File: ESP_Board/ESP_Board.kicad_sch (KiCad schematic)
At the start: 49 parts, among them J1 USB_C_Receptacle_USB2.0_14P, J2 Conn_01x18_Pin, J3 Conn_01x18_Pin, SW1 SW_Push, SW2 SW_Push, U1 ESP32-S3, U2 AMS1117, U3 W25Q128JVSIQ, Y1 C1E-40.000-8-1010-R

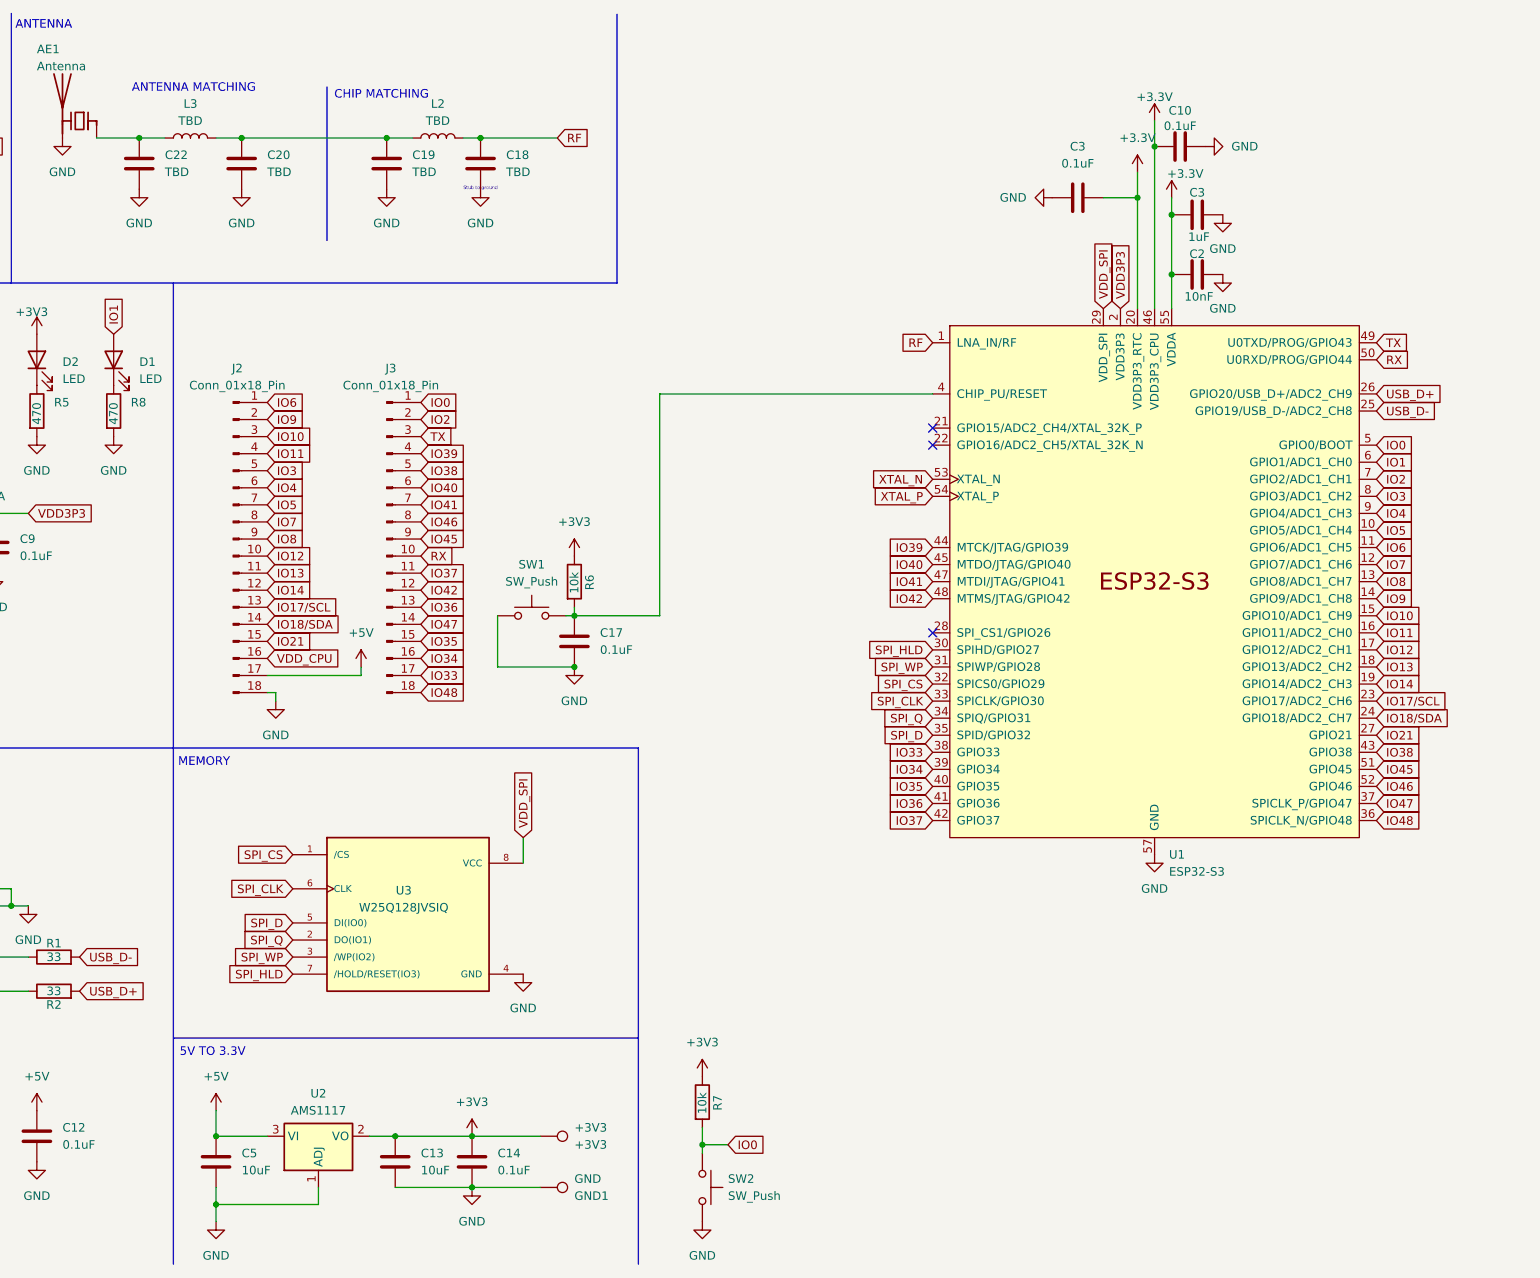
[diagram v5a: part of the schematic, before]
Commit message: Clean up schematic
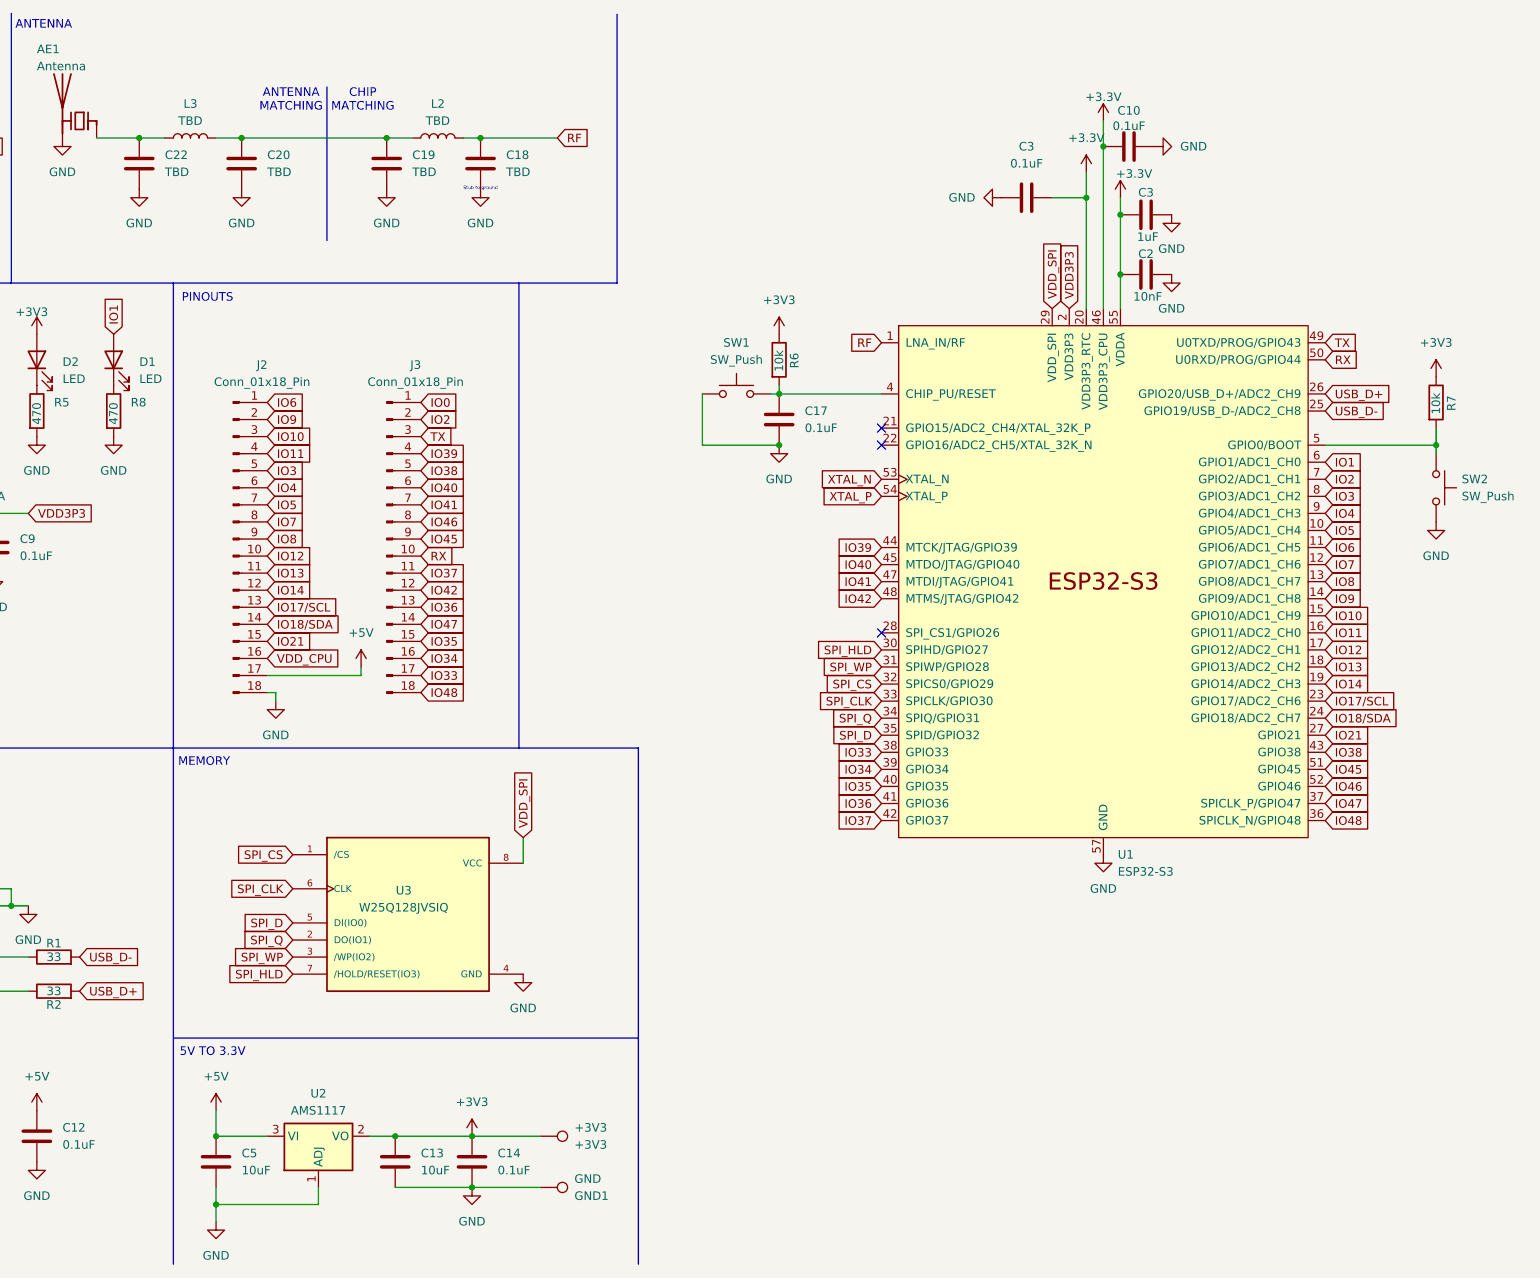
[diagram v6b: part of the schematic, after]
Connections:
- net IO0: no longer R7.2, SW2.1, U1.5 (GPIO0/BOOT)
- new net: R7.2, SW2.1, U1.5 (GPIO0/BOOT)
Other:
- note added: "PINOUTS"
- moved on the sheet: 1uF, C10, C17, C2, C3, R6, R7, SW1, SW2, U1

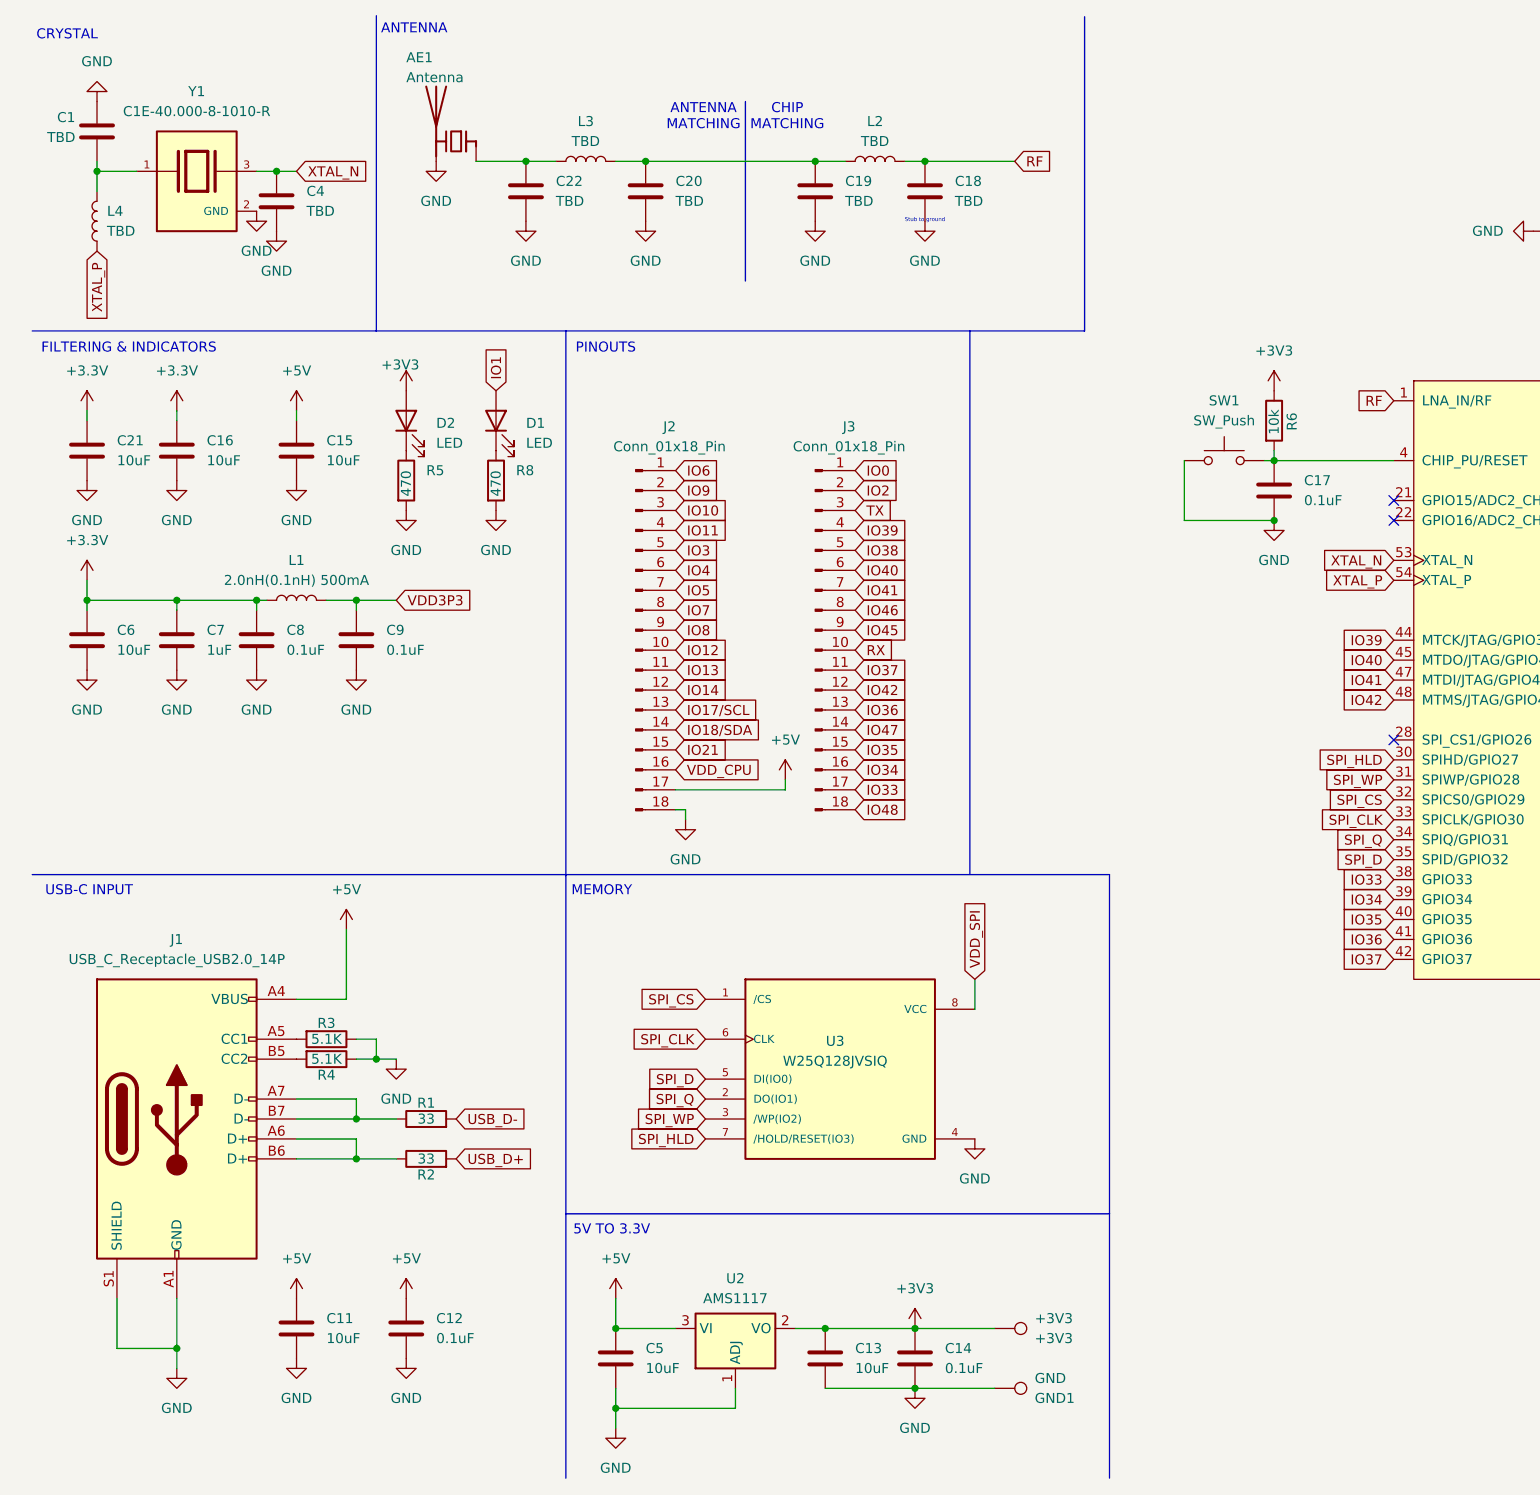
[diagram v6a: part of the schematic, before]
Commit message: Add 32k oscillator + antenna
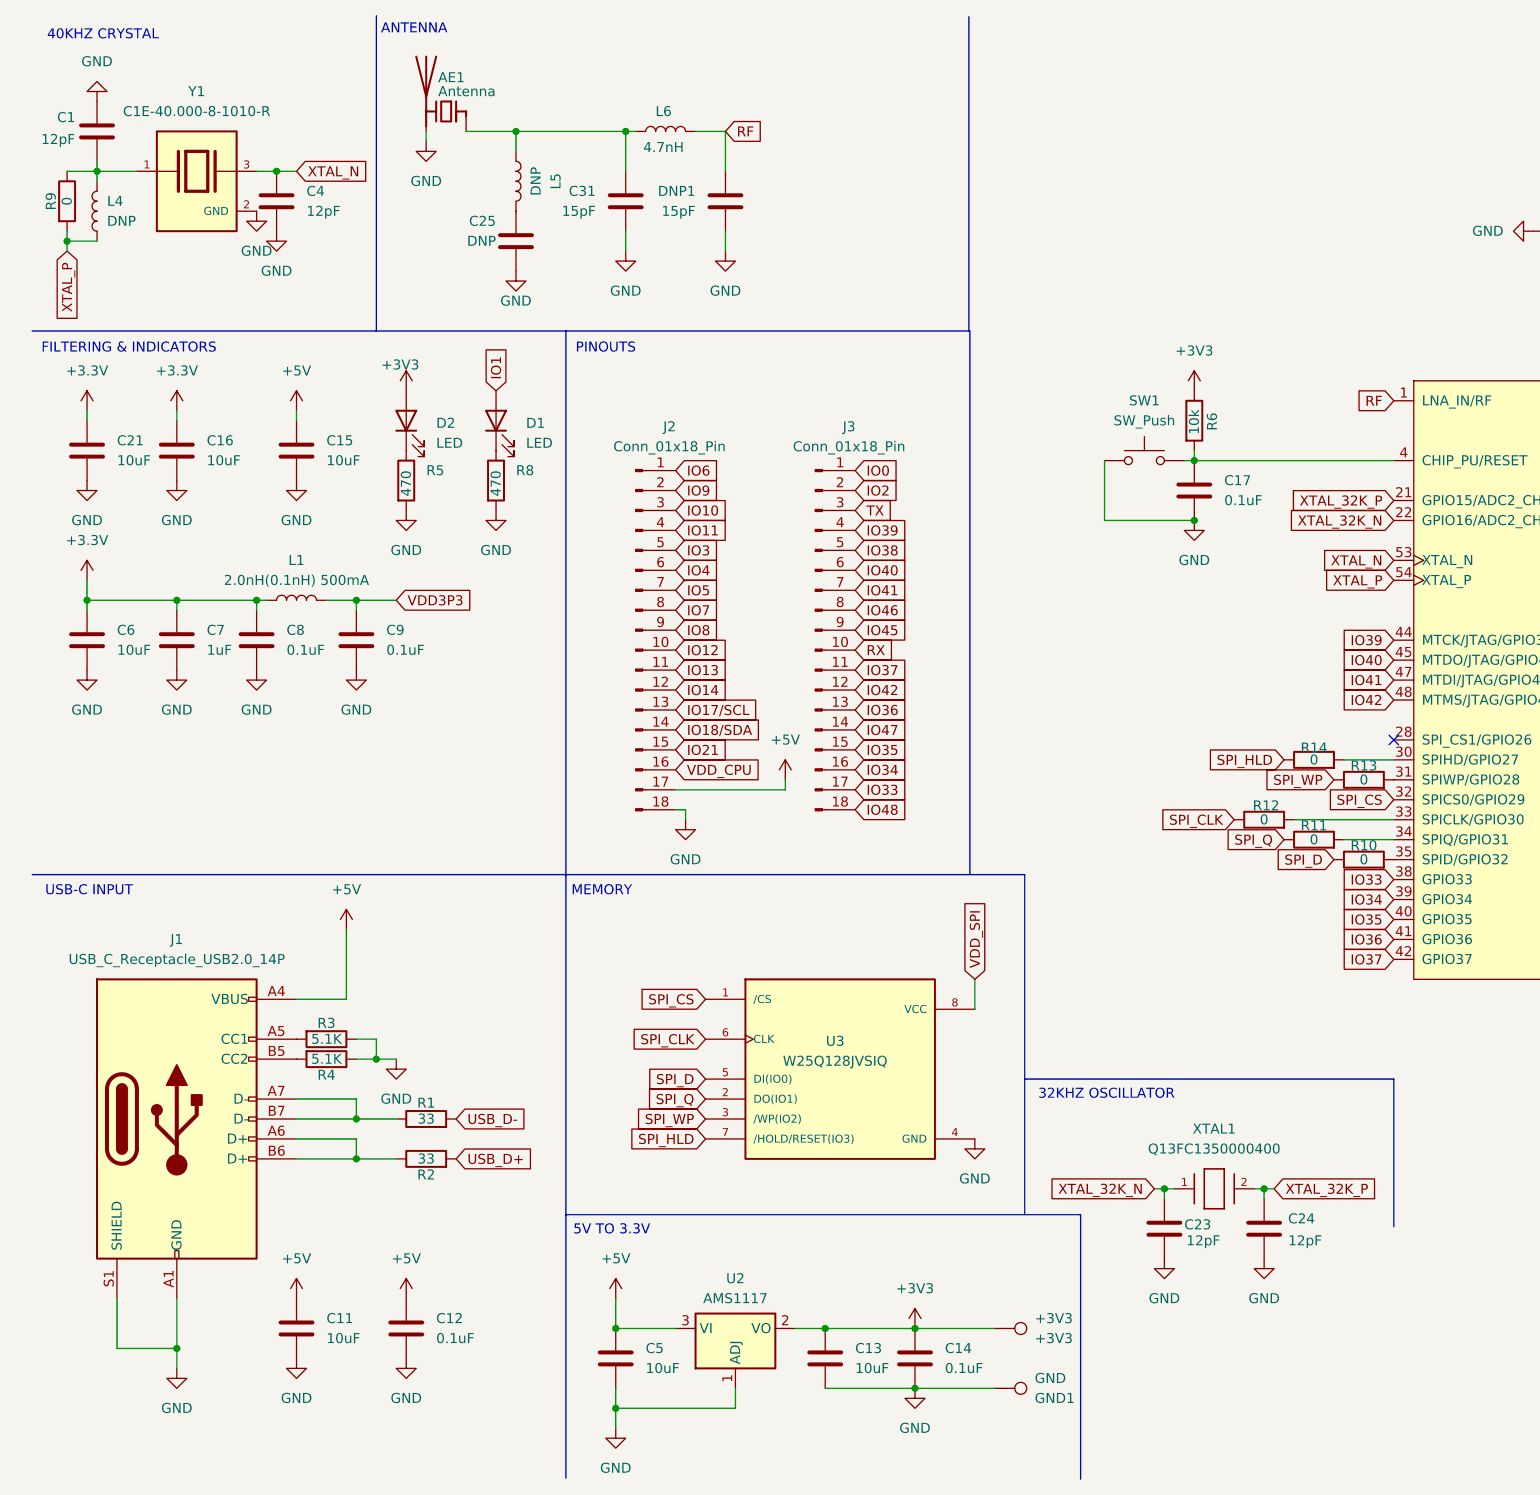
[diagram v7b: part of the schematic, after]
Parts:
- removed C18, C19, C20, C22: TBD, symbol Device:C
- removed L2, L3: TBD, symbol Device:L
- added C23, C24: 12pF, symbol Device:C
- added C25: DNP, Capacitor_SMD:C_0402_1005Metric, symbol Device:C
- added C31, DNP1: 15pF, Capacitor_SMD:C_0402_1005Metric, symbol Device:C
- added L5: DNP, Inductor_SMD:L_0402_1005Metric, symbol Device:L
- added L6: 4.7nH, Inductor_SMD:L_0402_1005Metric, symbol Device:L
- added R10, R11, R12, R13, R14, R9: 0, symbol Device:R
- added XTAL1: Q13FC1350000400, symbol Necessary_Imports:Q13FC1350000400
- C1, C4: value TBD -> 12pF
- L4: value TBD -> DNP
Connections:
- net GND: now also C23.2, C24.2, C25.2, C31.2, DNP1.2
- net RF: now also DNP1.1, L6.1
- net SPI_CLK: now also R12.1; no longer U1.33 (SPICLK/GPIO30)
- net SPI_D: now also R10.1; no longer U1.35 (SPID/GPIO32)
- net SPI_HLD: now also R14.1; no longer U1.30 (SPIHD/GPIO27)
- net SPI_Q: now also R11.1; no longer U1.34 (SPIQ/GPIO31)
- net SPI_WP: now also R13.1; no longer U1.31 (SPIWP/GPIO28)
- net XTAL_P: now also R9.2
- net at C1.2, L4.2, Y1.1: now also R9.1
- net at AE1.1 (FEED): now also C31.1, L5.2, L6.2
- net XTAL_32K_P: now reaches U1.21 (GPIO15/ADC2_CH4/XTAL_32K_P)
- net XTAL_32K_P: now also C24.1, XTAL1.2
- net XTAL_32K_N: now reaches U1.22 (GPIO16/ADC2_CH5/XTAL_32K_N)
- net XTAL_32K_N: now also C23.1, XTAL1.1
- new net: C25.1, L5.1
- new net: R14.2, U1.30 (SPIHD/GPIO27)
- new net: R11.2, U1.34 (SPIQ/GPIO31)
- new net: R12.2, U1.33 (SPICLK/GPIO30)
- new net: R10.2, U1.35 (SPID/GPIO32)
- new net: R13.2, U1.31 (SPIWP/GPIO28)
- no-connect marks 3 -> 1
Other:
- note added: "32KHZ OSCILLATOR"
- note added: "40KHZ CRYSTAL"
- note removed: "ANTENNA MATCHING"
- note removed: "CHIP MATCHING"
- note removed: "CRYSTAL"
- note removed: "Stub to ground"
- company: (none) -> UTRA ART
- title: (none) -> ESP32-S3 Board
- moved on the sheet: AE1, C17, L4, R6, SW1

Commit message: Update with fault monitor peripherals
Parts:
- added D3 (x2), D4 (x2): LED, LED_THT:LED_D5.0mm, symbol Device:LED
- added J4, J5, J6: Conn_01x02, TerminalBlock:TerminalBlock_MaiXu_MX126-5.0-02P_1x02_P5.00mm, symbol Connector_Generic:Conn_01x02
- added J4: Conn_01x03, TerminalBlock:TerminalBlock_MaiXu_MX126-5.0-03P_1x03_P5.00mm, symbol Connector_Generic:Conn_01x03
- added J5: Conn_01x02, Connector_PinHeader_2.54mm:PinHeader_1x02_P2.54mm_Vertical, symbol Connector_Generic:Conn_01x02
- added J6, J7: Conn_01x06, TerminalBlock:TerminalBlock_MaiXu_MX126-5.0-06P_1x06_P5.00mm, symbol Connector_Generic:Conn_01x06
- added R15, R16, R17, R18: 2.2k, Resistor_THT:R_Axial_DIN0207_L6.3mm_D2.5mm_P10.16mm_Horizontal, symbol Device:R
- added R19, R20: 10k, Resistor_THT:R_Axial_DIN0207_L6.3mm_D2.5mm_P10.16mm_Horizontal, symbol Device:R
- added RV1: 10K, DigiKey:POT_N6L30T0N_AMP, symbol Device:R_Potentiometer
- added TP1: TestPoint, Connector_PinHeader_2.54mm:PinHeader_1x01_P2.54mm_Vertical, symbol Connector:TestPoint
- added U4: ~, Package_TO_SOT_THT:TO-92L, symbol ProPrj_Fau-easyedapro:DS18B20T(XBLW)
- +3V3, AE1, C25, GND, L4, L5: PARTNO (none) -> N/A
- C1, C23, C24, C4: PARTNO (none) -> 0805CG120J500NT
- C10, C12, C14, C17, C3, C8, C9: PARTNO (none) -> CL21B104KCFNNNE
- C11, C13, C15, C16, C21, C5, C6: PARTNO (none) -> CL21A106KAYNNNE
- C2: PARTNO (none) -> CL21B103KBANNNC
- C3: renamed from 1uF; value C3 -> 1uF; PARTNO (none) -> CL21B105KBFNNNE
- C31, DNP1: PARTNO (none) -> CC0805JRNPO9BN150
- C7: PARTNO (none) -> CL21B105KBFNNNE
- D1: PARTNO (none) -> NCD0603Y2
- D2: PARTNO (none) -> NCD0805R1
- R10, R11, R12, R13, R14, R9: PARTNO (none) -> 0805W8F0000T5E
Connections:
- net +5V: now also J4.1 (Pin_1), J4.1 (Pin_1), R19.1, R20.1, U4.3 (VDD)
- net GND: now also D3.1 (K), D3.1 (K), D4.1 (K), D4.1 (K), J4.2 (Pin_2), J4.2 (Pin_2), U4.1 (GND)
- net IO0: now also J7.6 (Pin_6)
- net IO12: now also U4.2 (DQ)
- net IO13: now also J6.5 (Pin_5), R20.2
- net IO14: now also J4.3 (Pin_3)
- net IO2: now also J6.6 (Pin_6), R19.2
- net IO21: now also J7.2 (Pin_2)
- net IO33: now also R17.1
- net IO34: now also J6.1 (Pin_1)
- net IO4: now also J7.5 (Pin_5)
- net IO5: now also J5.1 (Pin_1)
- net RX: now also J6.2 (Pin_2)
- net TX: now also J6.1 (Pin_1)
- new net: D4.2 (A), R18.2
- new net: J5.2 (Pin_2), RV1.2, TP1.1
- new net: D3.2 (A), R17.2
- new net: D3.2 (A), R15.2
- new net: D4.2 (A), R16.2
- new net: J5.1 (Pin_1), RV1.3
- new net: J5.2 (Pin_2), RV1.1
- new net IO15: J6.2 (Pin_2)
- new net IO16: J6.3 (Pin_3)
- new net IO17: J7.4 (Pin_4)
- new net IO18: J7.3 (Pin_3)
- new net IO19: J6.4 (Pin_4)
- new net IO22: J7.1 (Pin_1)
- new net IO25: R16.1
- new net IO26: R15.1
- new net IO32: R18.1
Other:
- note added: "SENSORS"
- moved on the sheet: C23, C24, XTAL1
